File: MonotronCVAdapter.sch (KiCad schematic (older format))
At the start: 8 parts, among them J1 Conn_01x04_Female, J2 Pitch, J3 Gate, Q1 BC557

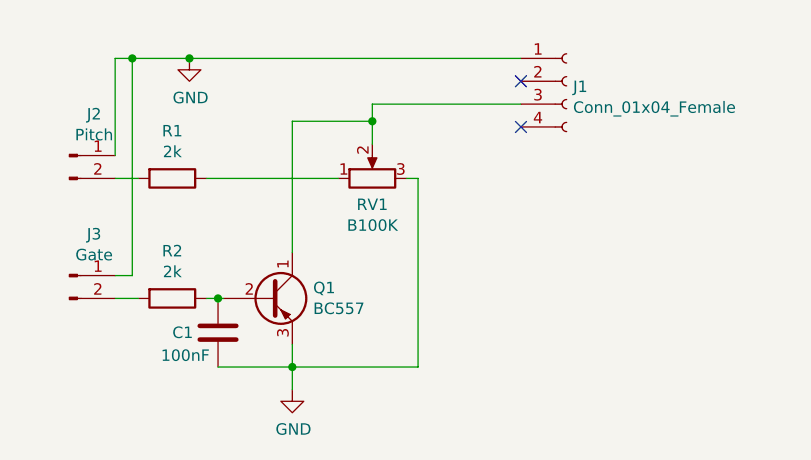
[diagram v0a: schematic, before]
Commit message: Adding PDF of schematic
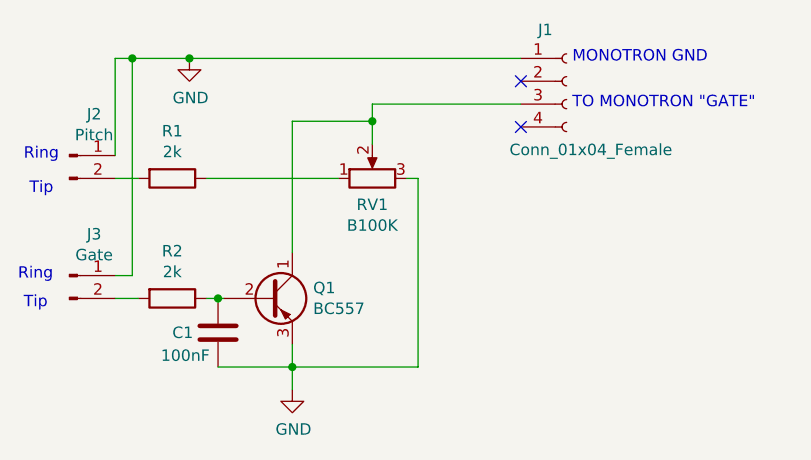
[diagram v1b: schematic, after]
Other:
- note added: "MONOTRON GND"
- note added: "Ring"
- note added: "TO MONOTRON "GATE""
- note added: "Tip"
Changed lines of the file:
@@
 EESchema Schematic File Version 4
+LIBS:MonotronCVAdapter-cache
 EELAYER 29 0
 EELAYER END
@@
 U 1 1 5D1BC1E3
 P 6400 3325
-F 0 "J1" H 6428 3301 50  0000 L CNN
-F 1 "Conn_01x04_Female" H 6428 3210 50  0000 L CNN
+F 0 "J1" H 6275 3550 50  0000 L CNN
+F 1 "Conn_01x04_Female" H 6150 3025 50  0000 L CNN
 F 2 "Pin_Headers:Pin_Header_Straight_1x04_Pitch2.54mm" H 6400 3325 50  0001 C CNN
 F 3 "~" H 6400 3325 50  0001 C CNN
@@
 Wire Wire Line
 	4825 3750 5400 3750
+Text Notes 4050 3825 0    50   ~ 0
+Tip
+Text Notes 4025 3675 0    50   ~ 0
+Ring
+Text Notes 4025 4325 0    50   ~ 0
+Tip
+Text Notes 4000 4200 0    50   ~ 0
+Ring
+Text Notes 6425 3250 0    50   ~ 0
+MONOTRON GND
+Text Notes 6425 3450 0    50   ~ 0
+TO MONOTRON "GATE"
 $EndSCHEMATC
